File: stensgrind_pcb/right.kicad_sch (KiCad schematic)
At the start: 118 parts, among them J5 SERIAL_01, J6 Conn_01x04_Pin, SW24 SW_PUSH, SW25 SW_PUSH, SW26 SW_PUSH, SW27 SW_PUSH, SW28 SW_PUSH, SW29 SW_PUSH, SW30 SW_PUSH, SW31 SW_PUSH, SW32 SW_PUSH, SW33 SW_PUSH, SW34 SW_PUSH, SW35 SW_PUSH, SW36 SW_PUSH, SW37 SW_PUSH, SW38 SW_PUSH, SW39 SW_PUSH, SW40 SW_PUSH, SW41 SW_PUSH, SW42 SW_PUSH, SW43 SW_PUSH, SW44 SW_PUSH, SW45 SW_PUSH, SW46 SW_PUSH, U27 ProMicro_r, U28 ISO1050DUB, U29 CAHCT1G125QDCKRQ1, U30 4492, U31 4492, U32 4492, U33 4492, U34 4492, U35 4492, U36 4492, U37 4492, U38 4492, U39 4492, U40 4492, U41 4492, U42 4492, U43 4492, U44 4492, U45 4492, U46 4492, U47 4492, U48 4492, U49 4492, U50 4492, U51 4492, U52 4492

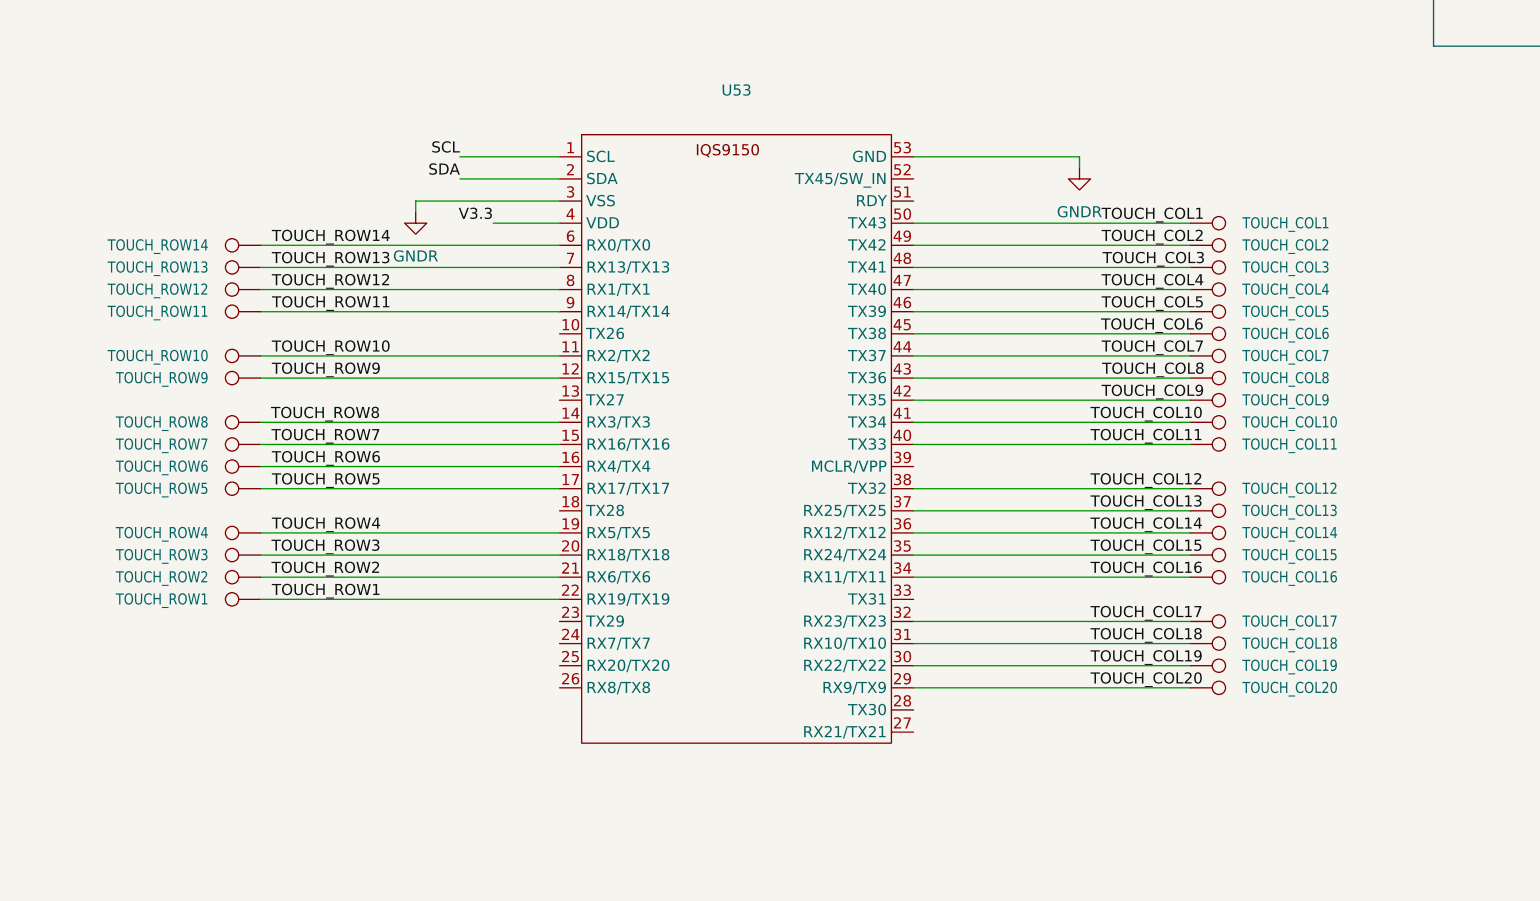
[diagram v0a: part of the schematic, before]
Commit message: ofcourse we are adding a touchpad
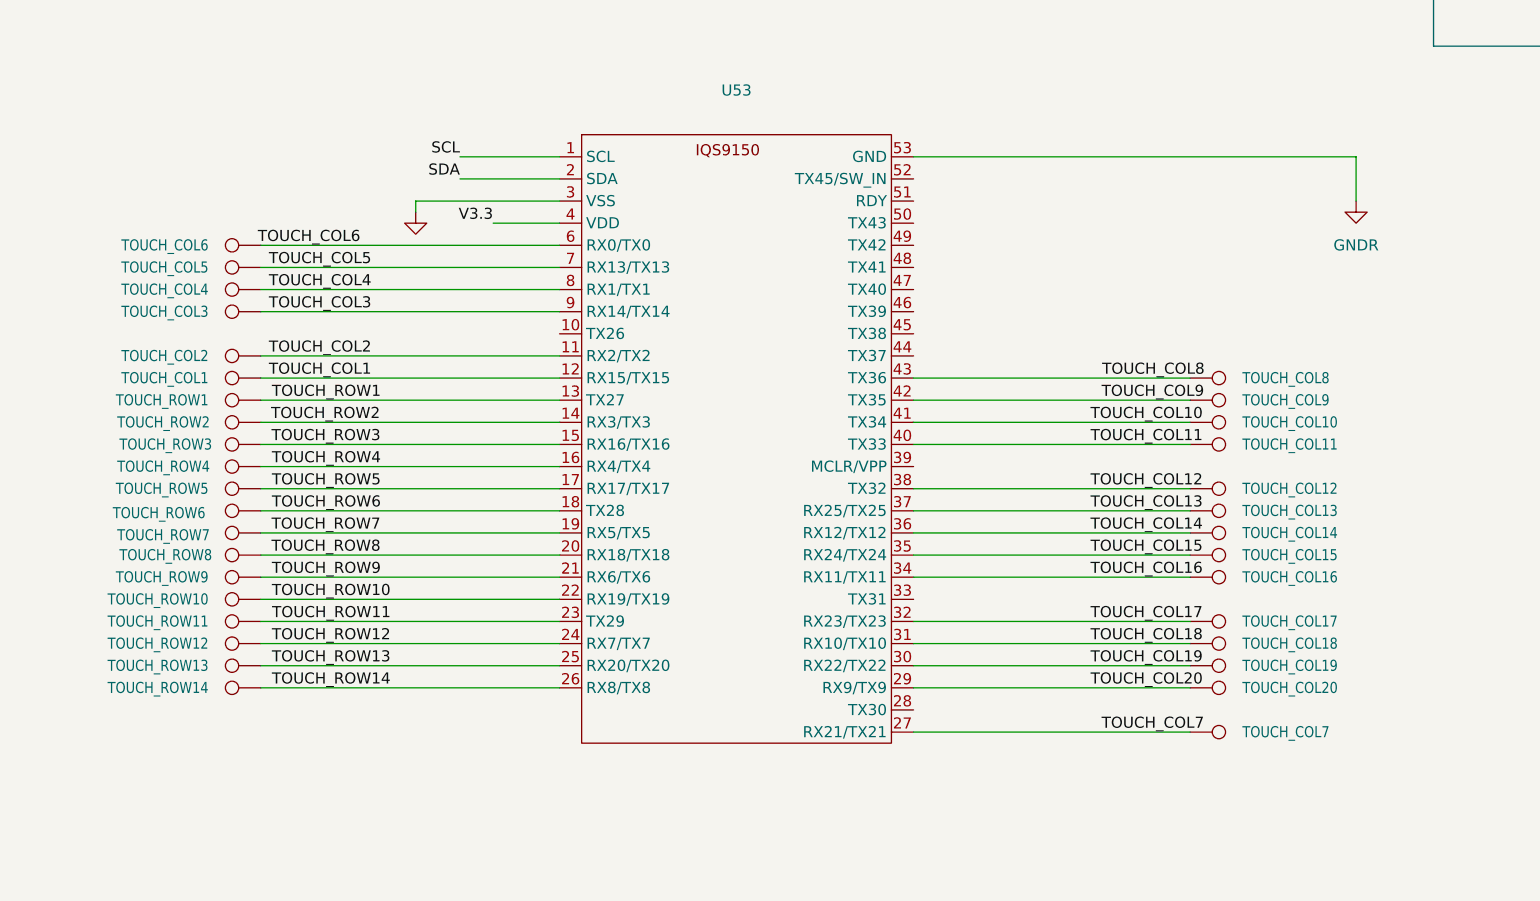
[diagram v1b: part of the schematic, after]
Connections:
- net TOUCH_COL1: now also U53.12 (RX15/TX15); no longer U53.50 (TX43)
- net TOUCH_COL2: now also U53.11 (RX2/TX2); no longer U53.49 (TX42)
- net TOUCH_COL3: now also U53.9 (RX14/TX14); no longer U53.48 (TX41)
- net TOUCH_COL4: now also U53.8 (RX1/TX1); no longer U53.47 (TX40)
- net TOUCH_COL5: now also U53.7 (RX13/TX13); no longer U53.46 (TX39)
- net TOUCH_COL6: now also U53.6 (RX0/TX0); no longer U53.45 (TX38)
- net TOUCH_COL7: now also U53.27 (RX21/TX21); no longer U53.44 (TX37)
- net TOUCH_ROW1: now also U53.13 (TX27); no longer U53.22 (RX19/TX19)
- net TOUCH_ROW10: now also U53.22 (RX19/TX19); no longer U53.11 (RX2/TX2)
- net TOUCH_ROW11: now also U53.23 (TX29); no longer U53.9 (RX14/TX14)
- net TOUCH_ROW12: now also U53.24 (RX7/TX7); no longer U53.8 (RX1/TX1)
- net TOUCH_ROW13: now also U53.25 (RX20/TX20); no longer U53.7 (RX13/TX13)
- net TOUCH_ROW14: now also U53.26 (RX8/TX8); no longer U53.6 (RX0/TX0)
- net TOUCH_ROW2: now also U53.14 (RX3/TX3); no longer U53.21 (RX6/TX6)
- net TOUCH_ROW3: now also U53.15 (RX16/TX16); no longer U53.20 (RX18/TX18)
- net TOUCH_ROW4: now also U53.16 (RX4/TX4); no longer U53.19 (RX5/TX5)
- net TOUCH_ROW6: now also U53.18 (TX28); no longer U53.16 (RX4/TX4)
- net TOUCH_ROW7: now also U53.19 (RX5/TX5); no longer U53.15 (RX16/TX16)
- net TOUCH_ROW8: now also U53.20 (RX18/TX18); no longer U53.14 (RX3/TX3)
- net TOUCH_ROW9: now also U53.21 (RX6/TX6); no longer U53.12 (RX15/TX15)
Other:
- moved on the sheet: TOUCH_COL1, TOUCH_COL2, TOUCH_COL3, TOUCH_COL4, TOUCH_COL5, TOUCH_COL6, TOUCH_COL7, TOUCH_ROW1, TOUCH_ROW10, TOUCH_ROW11, TOUCH_ROW12, TOUCH_ROW13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

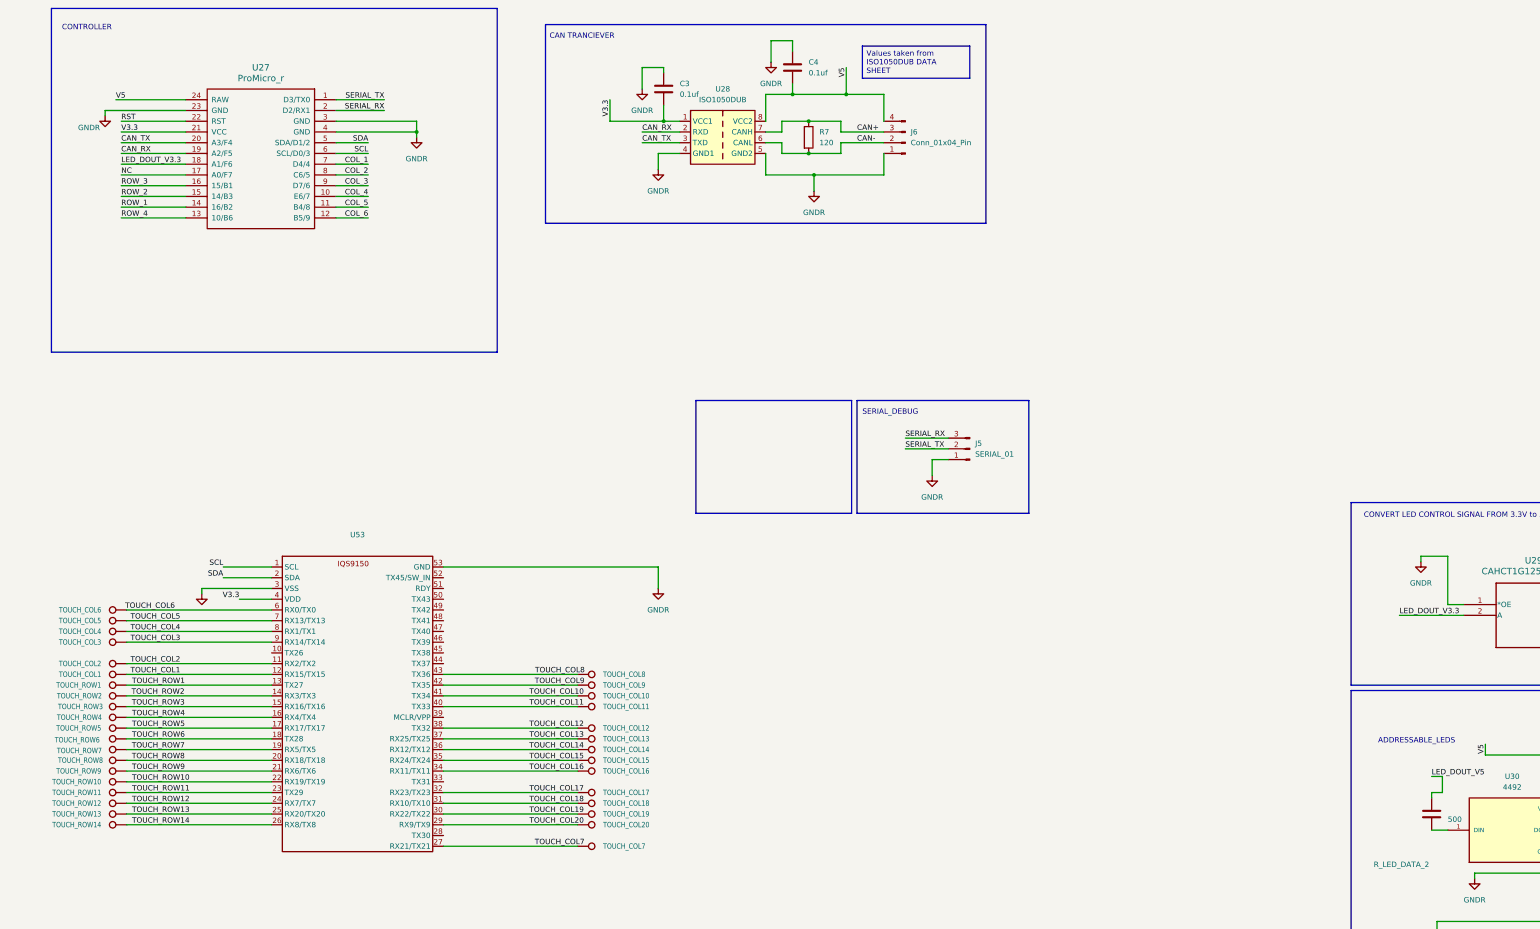
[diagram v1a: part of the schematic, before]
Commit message: Remove touchpad from main board, expose i2c instead
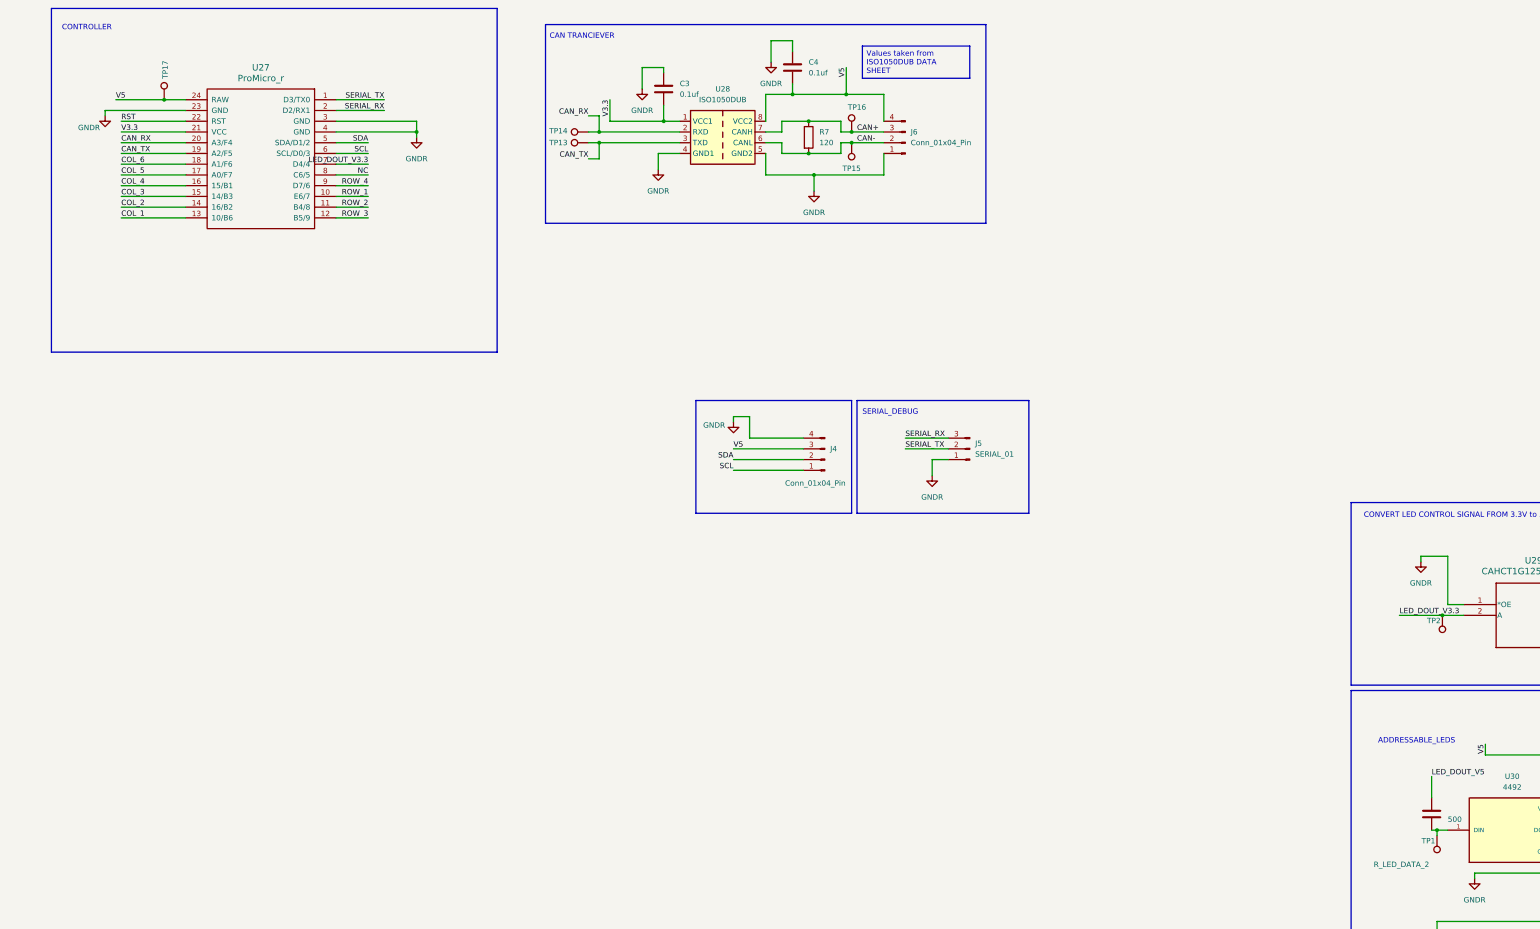
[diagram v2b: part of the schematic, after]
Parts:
- removed TOUCH_COL1, TOUCH_COL10, TOUCH_COL11, TOUCH_COL12, TOUCH_COL13, TOUCH_COL14, TOUCH_COL15, TOUCH_COL16, TOUCH_COL17, TOUCH_COL18, TOUCH_COL19, TOUCH_COL2, TOUCH_COL20, TOUCH_COL3, TOUCH_COL4, TOUCH_COL5, TOUCH_COL6, TOUCH_COL7, TOUCH_COL8, TOUCH_COL9: TESTPOINTPAD_0_5MM, TestPoint:TestPoint_Pad_D1.0mm, symbol Connector:TestPoint
- removed TOUCH_ROW1, TOUCH_ROW10, TOUCH_ROW11, TOUCH_ROW12, TOUCH_ROW13, TOUCH_ROW14, TOUCH_ROW2, TOUCH_ROW3, TOUCH_ROW4, TOUCH_ROW5, TOUCH_ROW6, TOUCH_ROW7, TOUCH_ROW8, TOUCH_ROW9: TESTPOINTPAD_0_5MM, Touchpad:PAD_0_5MM, symbol Connector:TestPoint
- removed U53: ~, Package_DFN_QFN:IQS9150, symbol DEV-18288:IQS9150
- added J4: Conn_01x04_Pin, Connector_PinSocket_2.54mm:PinSocket_1x04_P2.54mm_Vertical, symbol Connector:Conn_01x04_Pin
- added TP1, TP13, TP14, TP15, TP16, TP17, TP2: 0.5mm, PCM_SparkFun-Connector:TestPoint-0.5mm, symbol PCM_SparkFun-Connector:TestPoint_0.5mm
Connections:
- net CAN+: now also TP16.1
- net CAN-: now also TP15.1
- net CAN_RX: now also U27.20 (A3/F4), TP14.1; no longer U27.19 (A2/F5)
- net CAN_TX: now also U27.19 (A2/F5), TP13.1; no longer U27.20 (A3/F4)
- net COL_1: now also U27.13 (10/B6); no longer U27.7 (D4/4)
- net COL_2: now also U27.14 (16/B2); no longer U27.8 (C6/5)
- net COL_3: now also U27.15 (14/B3); no longer U27.9 (D7/6)
- net COL_4: now also U27.16 (15/B1); no longer U27.10 (E6/7)
- net COL_5: now also U27.17 (A0/F7); no longer U27.11 (B4/8)
- net COL_6: now also U27.18 (A1/F6); no longer U27.12 (B5/9)
- net GNDR: now also J4.4 (Pin_4)
- net LED_DOUT_V3.3: now also U27.7 (D4/4), TP2.1; no longer U27.18 (A1/F6)
- net NC: now also U27.8 (C6/5); no longer U27.17 (A0/F7)
- net ROW_1: now also U27.10 (E6/7); no longer U27.14 (16/B2)
- net ROW_2: now also U27.11 (B4/8); no longer U27.15 (14/B3)
- net ROW_3: now also U27.12 (B5/9); no longer U27.16 (15/B1)
- net ROW_4: now also U27.9 (D7/6); no longer U27.13 (10/B6)
- net SCL: now also J4.1 (Pin_1)
- net SDA: now also J4.2 (Pin_2)
- net V5: now also J4.3 (Pin_3), TP17.1
- net at R_LED_DATA_2.1, U30.1 (DIN): now also TP1.1

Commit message: finish up v1
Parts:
- removed TP15, TP16: 0.5mm, PCM_SparkFun-Connector:TestPoint-0.5mm, symbol PCM_SparkFun-Connector:TestPoint_0.5mm
- added D47: LED, LED_SMD:LED_1206_3216Metric, symbol Device:LED
- added R11: R, Resistor_SMD:R_1206_3216Metric_Pad1.30x1.75mm_HandSolder, symbol Device:R
- added TP3: 0.5mm, PCM_SparkFun-Connector:TestPoint-0.5mm, symbol PCM_SparkFun-Connector:TestPoint_0.5mm
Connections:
- net GNDR: now also R11.2
- net NC renamed STATUS_LED
- net STATUS_LED: now also D47.2 (A), TP3.1
- new net: D47.1 (K), R11.1
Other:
- note added: "ACTIVE IF CONNECTION TO OTHER SIDE IS ESTABLISHED"
- note added: "STATUS LED"
- moved on the sheet: J4, J5, TP2

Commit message: fix i2c mapping
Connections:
- net SCL: now also J4.2 (Pin_2); no longer J4.1 (Pin_1)
- net SDA: now also J4.1 (Pin_1); no longer J4.2 (Pin_2)
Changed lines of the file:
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@@
 	)
 	(label "SCL"
-		(at 154.94 134.62 180)
+		(at 154.94 132.08 180)
 		(effects
 			(font
@@
 	)
 	(label "SDA"
-		(at 154.94 132.08 180)
-		(effects
-			(font
+		(at 154.94 134.62 180)
+		(effects
+			(font
